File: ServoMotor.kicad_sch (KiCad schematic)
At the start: 12 parts, among them J5 DE9_Socket_MountingHoles, U13 ISO6763DWR, U15 TCAN1051DRQ1, U17 ESD2CANFD24DBZRQ1

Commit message: Redesign schematic for dual motor encoders
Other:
- note added: "CAN ESD protection"
- note added: "CAN transceiver"
- note added: "Digital isolator"
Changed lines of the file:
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@@
 		(title "Elevation Control_Gigabit")
 		(date "2026-09-01")
-		(rev "Sep_2026_V1")
+		(rev "P3 REVIEW")
 		(company "Starspec")
 		(comment 4 "Mauro M. Coutinho")
+	)
+	(text "CAN ESD protection"
+		(exclude_from_sim no)
+		(at 233.68 19.05 0)
+		(effects
+			(font
+				(size 1.27 1.27)
+			)
+		)
+	)
+	(text "Digital isolator"
+		(exclude_from_sim no)
+		(at 73.66 57.15 0)
+		(effects
+			(font
+				(size 1.27 1.27)
+			)
+		)
 	)
 	(text "The existing TSM24A devices can work at 1 Mbit/s, but \nthey have much higher capacitance and are not CAN-specific."
 		(exclude_from_sim no)
 		(at 329.184 56.642 0)
+		(effects
+			(font
+				(size 1.27 1.27)
+			)
+		)
+	)
+	(text "CAN transceiver"
+		(exclude_from_sim no)
+		(at 181.61 67.31 0)
 		(effects
 			(font
@@
 		(property "ALT_LCSC" "C190987"
 			(at 161.29 81.28 0)
-			(effects (font (size 1.27 1.27)) (hide yes))
+			(effects
+				(font
+					(size 1.27 1.27)
+				)
+				(hide yes)
+			)
 		)
 		(property "ALT_MANUFACTURER_PART_NUMBER" "TCAN1051HGVDRQ1"
 			(at 161.29 81.28 0)
-			(effects (font (size 1.27 1.27)) (hide yes))
+			(effects
+				(font
+					(size 1.27 1.27)
+				)
+				(hide yes)
+			)
 		)
 		(pin "1"

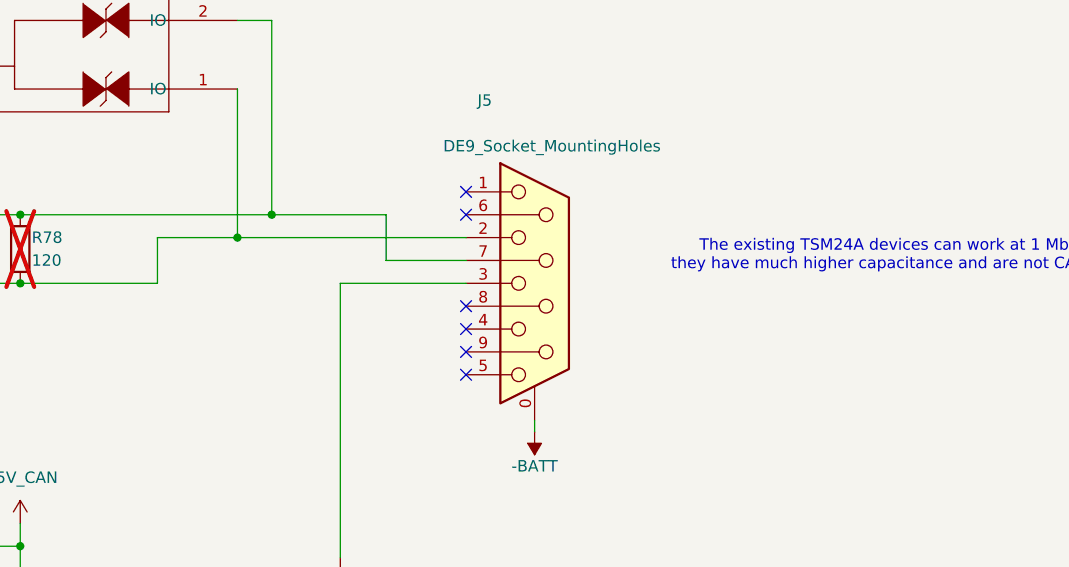
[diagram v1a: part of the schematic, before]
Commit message: Preserve P5 equal-size placement, controller stack and native BOM
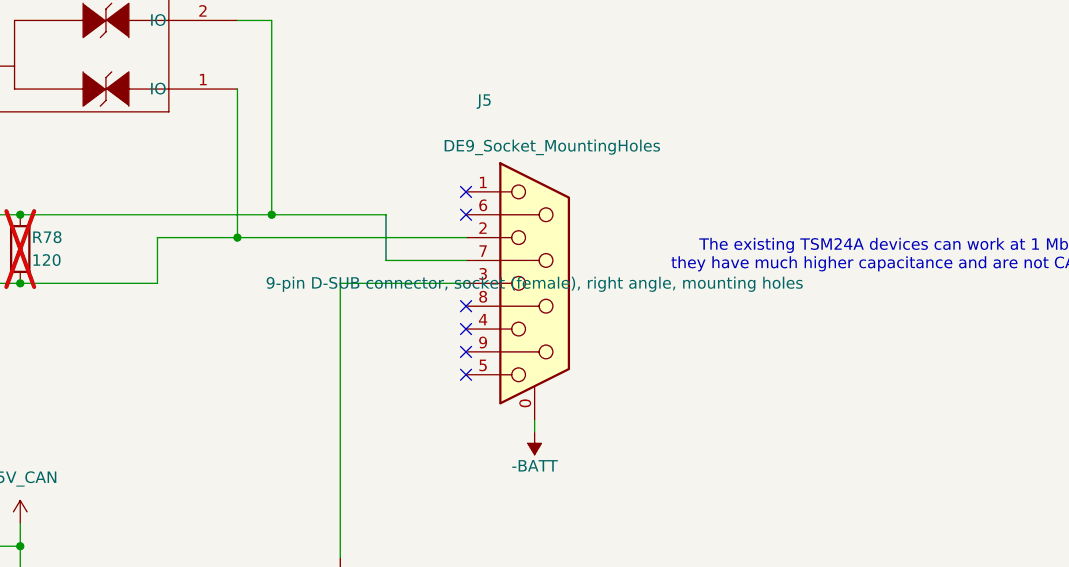
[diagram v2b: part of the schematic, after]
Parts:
- C59, C60, C66, C68: Assembly (none) -> FIT; BOM Status (none) -> PART IDENTIFIED; sourcing/footprint review pending; Footprint Status (none) -> Assigned; drawing/pad verification pending; Function (none) -> Unpolarized capacitor; JLCPCB Status (none) -> Historical ID; recheck exact part and assembly availability; MPN (none) -> CL21B104KCFNNNE; Supplier Data Checked (none) -> UNDATED legacy record; Supplier Source (none) -> Legacy schematic record; exact supplier listing verificatio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; Temp Basis (none) -> Legacy rating; ambient/junction basis unverified; Temp Max (degC) (none) -> 125; Temp Min (degC) (none) -> -55; Temp Source (none) -> Legacy schematic field; primary-source verification pending; Temp Status (none) -> Inherited rating; system requirement pending
- C67: Assembly (none) -> FIT; BOM Status (none) -> PART IDENTIFIED; sourcing/footprint review pending; Footprint Status (none) -> Assigned; drawing/pad verification pending; Function (none) -> Unpolarized capacitor; JLCPCB Status (none) -> Historical ID; recheck exact part and assembly availability; MPN (none) -> CL32B475KCVZNWE; Supplier Data Checked (none) -> UNDATED legacy record; Supplier Source (none) -> Legacy schematic record; exact supplier listing verificatio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; Temp Basis (none) -> Legacy rating; ambient/junction basis unverified; Temp Max (degC) (none) -> 125; Temp Min (degC) (none) -> -55; Temp Source (none) -> Legacy schematic field; primary-source verification pending; Temp Status (none) -> Inherited rating; system requirement pending
- J5: Assembly (none) -> FIT; BOM Review (none) -> Same MPN as existing DE9 connectors. Verify exact pin grid,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; BOM Status (none) -> PART IDENTIFIED; sourcing/footprint review pending; Footprint Status (none) -> REVIEW: compare exact TE drawing to generic KiCad footprint; Function (none) -> DE9 female right-angle PCB connector; JLCPCB Library (none) -> UNVERIFIED; JLCPCB Status (none) -> LCSC exact match; JLC assembly availability unverified; MPN (none) -> 5747844-4; Supplier Data Checked (none) -> 2026-10-03; Supplier Source (none) -> https://www.lcsc.com/de/product-detail/C305941.html; Temp Basis (none) -> Operating; Temp Checked (none) -> 2026-10-03; Temp Max (degC) (none) -> 105; Temp Min (degC) (none) -> -55; Temp Source (none) -> https://www.te.com/en/product-5747844-4.html; Temp Status (none) -> Manufacturer rating recorded; system requirement pending
- R41, R42: Assembly (none) -> FIT; BOM Status (none) -> PART IDENTIFIED; sourcing/footprint review pending; Footprint Status (none) -> Assigned; drawing/pad verification pending; Function (none) -> Resistor; JLCPCB Status (none) -> Historical ID; recheck exact part and assembly availability; MPN (none) -> RC0805FR-0710KL; Supplier Data Checked (none) -> UNDATED legacy record; Supplier Source (none) -> Legacy schematic record; exact supplier listing verificatio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; Temp Basis (none) -> Legacy rating; ambient/junction basis unverified; Temp Max (degC) (none) -> 155; Temp Min (degC) (none) -> -55; Temp Source (none) -> Legacy schematic field; primary-source verification pending; Temp Status (none) -> Inherited rating; system requirement pending
- R78: Assembly (none) -> DNP - not purchased; BOM Status (none) -> DNP; Footprint Status (none) -> Assigned; drawing/pad verification pending; Function (none) -> Resistor; JLCPCB Status (none) -> Historical ID; recheck exact part and assembly availability; MPN (none) -> RC0805FR-07120RL; Supplier Data Checked (none) -> UNDATED legacy record; Supplier Source (none) -> Legacy schematic record; exact supplier listing verificatio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; Temp Basis (none) -> Legacy rating; ambient/junction basis unverified; Temp Max (degC) (none) -> 155; Temp Min (degC) (none) -> -55; Temp Source (none) -> Legacy schematic field; primary-source verification pending; Temp Status (none) -> Inherited rating; system requirement pending
- U13: Assembly (none) -> FIT; BOM Status (none) -> PART IDENTIFIED; sourcing/footprint review pending; Footprint Status (none) -> Assigned; drawing/pad verification pending; Function (none) -> ISO6763DWR; JLCPCB Status (none) -> Historical ID; recheck exact part and assembly availability; MPN (none) -> ISO6763DWR; Supplier Data Checked (none) -> UNDATED legacy record; Supplier Source (none) -> Legacy schematic record; exact supplier listing verificatio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; Temp Basis (none) -> Legacy rating; ambient/junction basis unverified; Temp Max (degC) (none) -> 125; Temp Min (degC) (none) -> -40; Temp Source (none) -> Legacy schematic field; primary-source verification pending; Temp Status (none) -> Inherited rating; system requirement pending
- U15: Assembly (none) -> FIT; BOM Status (none) -> PART IDENTIFIED; sourcing/footprint review pending; Footprint Status (none) -> Assigned; drawing/pad verification pending; Function (none) -> TCAN1051DRQ1; JLCPCB Status (none) -> Historical ID; recheck exact part and assembly availability; MPN (none) -> TCAN1051DRQ1; Supplier Data Checked (none) -> UNDATED legacy record; Supplier Source (none) -> Legacy schematic record; exact supplier listing verificatio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; Temp Basis (none) -> Legacy rating; ambient/junction basis unverified; Temp Max (degC) (none) -> 125; Temp Min (degC) (none) -> -40; Temp Source (none) -> Legacy schematic field; primary-source verification pending; Temp Status (none) -> Inherited rating; system requirement pending
- U17: Assembly (none) -> FIT; BOM Status (none) -> PART IDENTIFIED; sourcing/footprint review pending; Footprint Status (none) -> Assigned; drawing/pad verification pending; Function (none) -> ESD2CANFD24DBZRQ1; JLCPCB Status (none) -> Historical ID; recheck exact part and assembly availability; MPN (none) -> ESD2CANFD24DBZRQ1; Supplier Data Checked (none) -> UNDATED legacy record; Supplier Source (none) -> Legacy schematic record; exact supplier listing verificatio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; Temp Basis (none) -> Legacy rating; ambient/junction basis unverified; Temp Max (degC) (none) -> 150; Temp Min (degC) (none) -> -55; Temp Source (none) -> Legacy schematic field; primary-source verification pending; Temp Status (none) -> Inherited rating; system requirement pending
